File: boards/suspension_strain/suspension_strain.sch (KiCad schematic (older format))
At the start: 84 parts, among them IC1 ATMEGA16M1, J1 micromatch_female_RA_18, J2 micromatch_female_RA_12, P1 CONN_02X03, U1 TPS561201, U2 CAN_Transceiver, U3 MCP6001RT, U4 MCP6001RT, U5 MCP6001RT, U6 MCP6001RT, U7 MCP6001RT, U8 MCP6001RT, Y1 Crystal_SMD

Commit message: updated schemetic and layout
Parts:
- added D4, D5: LED_0805, footprints:LED_0805_OEM, symbol LED_0805
- added R59, R60: R_200, footprints:R_0805_OEM, symbol R_200
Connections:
- net GND: now also D4.1 (K), D5.1 (K)
- net P_LED_1: now reaches IC1.8 ((PCINT0/MISO/PSCOUT2A)PB0)
- net P_LED_1: now also R59.1
- net P_LED_2: now reaches IC1.9 ((PCINT1/MOSI/PSCOUT2B)PB1)
- net P_LED_2: now also R60.1
- new net: D4.2 (A), R59.2
- new net: D5.2 (A), R60.2
- no-connect marks 14 -> 12

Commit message: final check
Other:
- note added: "Buck Convertor\n"
- note added: "CAN bus"
- note added: "Connectors\n"
- note added: "Programming LED"
- note added: "Strain Gauge Sensing"
- moved on the sheet: C1, C2, C7, C8, D4, D5, IC1, J1, J2, P1, R10, R11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

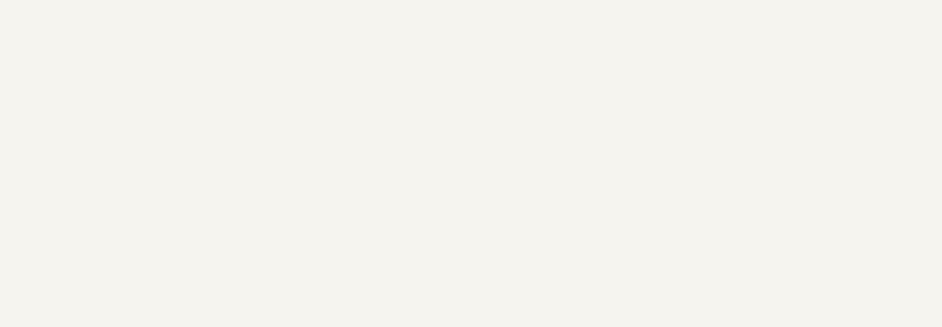
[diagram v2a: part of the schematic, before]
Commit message: adding PCB and schematic pdf
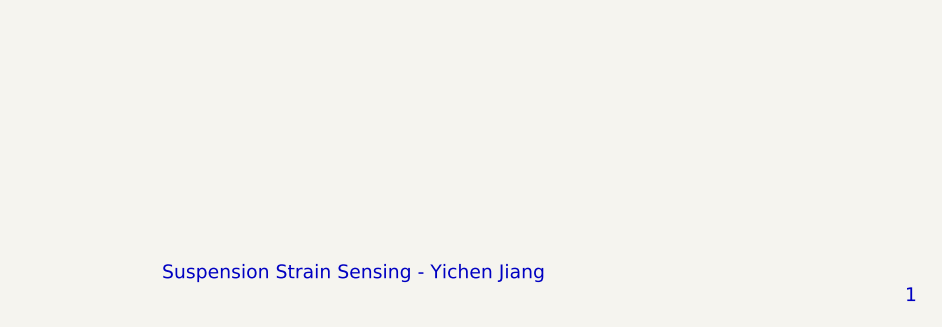
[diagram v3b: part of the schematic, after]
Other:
- note added: "1\n"
- note added: "Suspension Strain Sensing - Yichen Jiang"
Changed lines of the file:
@@
 Text Notes 4550 900  0    60   ~ 0
 Strain Gauge Sensing
+Text Notes 15900 10350 0    60   ~ 0
+1\n
+Text Notes 12650 10250 0    60   ~ 0
+Suspension Strain Sensing - Yichen Jiang
 $EndSCHEMATC

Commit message: adding cad for board
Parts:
- J2: symbol micromatch_female_RA_12 -> micromatch_female_RA_12-RESCUE-suspension_strain
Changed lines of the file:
@@
 EESchema Schematic File Version 2
+LIBS:suspension_strain-rescue
 LIBS:power
 LIBS:device
@@
 $EndComp
 $Comp
-L micromatch_female_RA_12 J2
+L micromatch_female_RA_12-RESCUE-suspension_strain J2
 U 1 1 59FC0B21
 P 2000 6450
